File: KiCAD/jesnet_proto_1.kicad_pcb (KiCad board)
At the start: 2 copper layers, 119.5 x 60.6 mm, 163 parts, among them J1 Conn_01x06_Female, J14 Conn_01x06, J15 Conn_01x06, J3 Conn_01x02, J4 Conn_01x01, J5 Rumble, J8 USB_B_Micro, Q1 Q_NMOS_GSD, Q2 Q_PMOS_GDS, Q3 Q_NMOS_GSD, SW1 A, SW10 Dup, SW11 Dright, SW12 Ddown, SW2 B, SW2 L, SW2 R, SW2 Z, SW3 X, SW4 Y, SW5 Start, SW6 L, SW7 R, SW9 Dleft, U1 MCP3202, U10 DRV5055A3xDBZxQ1, U11 DRV5055A3xDBZxQ1, U12 USBLC6-2P6, U13 USBLC6-2P6, U2 Stickbox_Assembly_Main, U3 MCP3202, U4 DRV5055A3xDBZxQ1, U5 Stickbox_Assembly_CStick, U6 AMS1117-3.3, U7 W25Q128JVS, U8 RP2040, U9 DRV5055A3xDBZxQ1, Y1 Crystal_GND24

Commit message: added 3d models to footprints, reversed polarity on trigger sliders
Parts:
- moved C7 2.01 mm to (123.3, 53.8), turned to 180 degrees
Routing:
- net /Lanalog: track 57.9 -> 70.8 mm
- net /Ranalog: track 30.9 -> 33.5 mm
- net GND: track 258.2 -> 256.9 mm

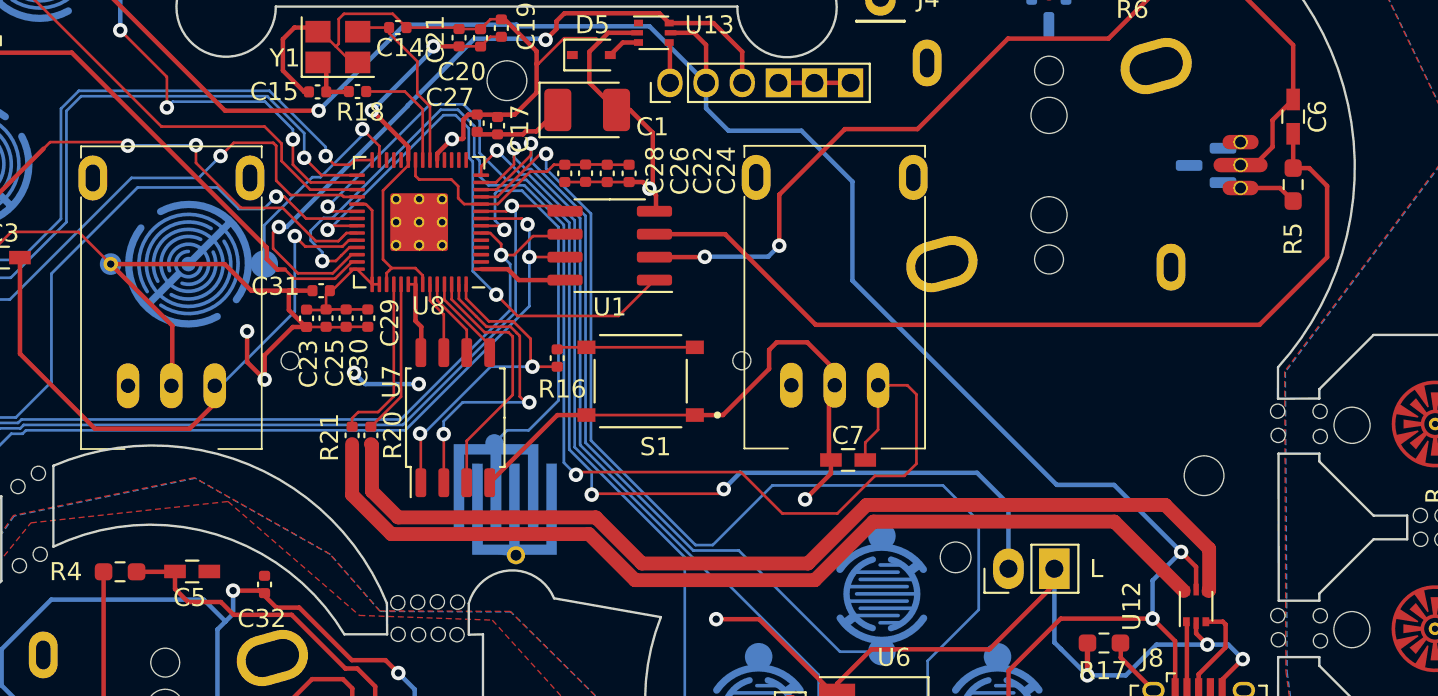
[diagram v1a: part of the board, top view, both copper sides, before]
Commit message: rerouted some traces, fixed 3d model of c0603
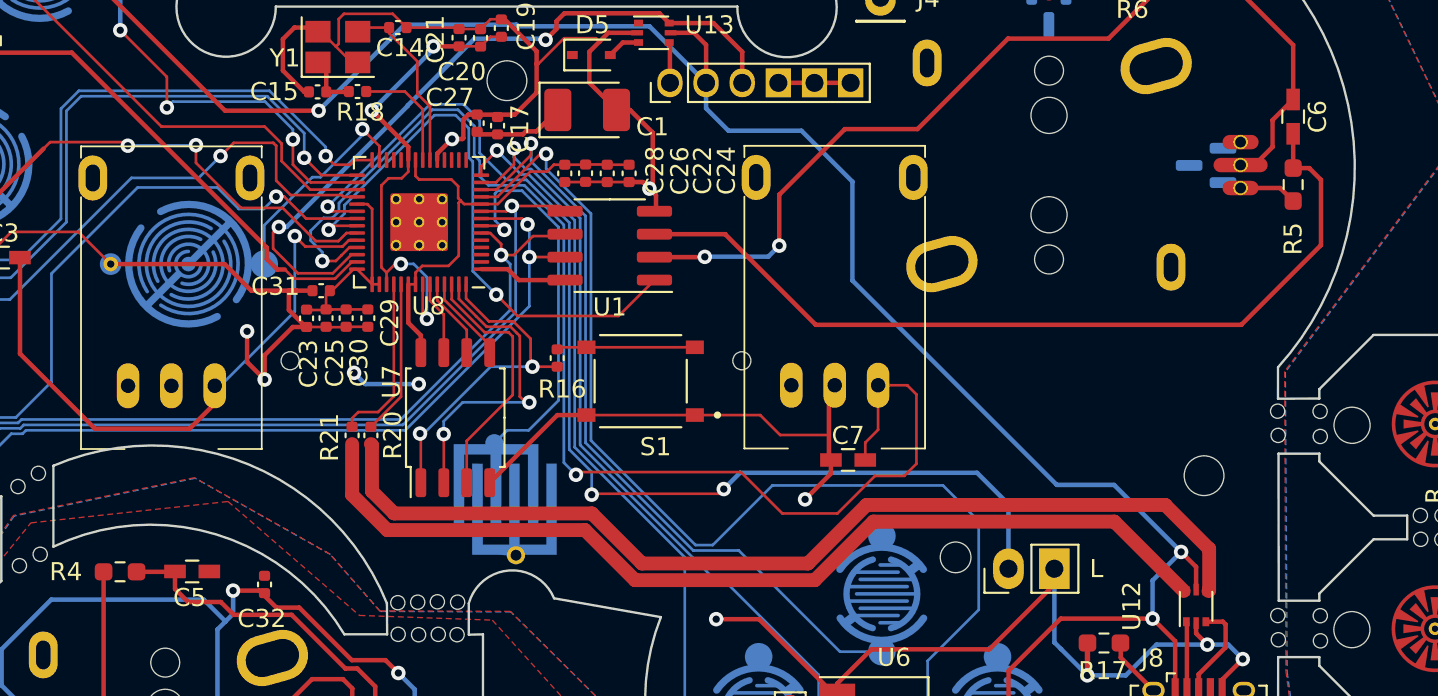
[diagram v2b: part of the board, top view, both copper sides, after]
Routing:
- net GND: track 256.9 -> 245.2 mm
- net +3V3: track 46.3 -> 53.0 mm
- net +1V1: track 22.7 -> 27.6 mm, vias 2 -> 4
- net /Stick_y_filt: track 49.0 -> 48.1 mm

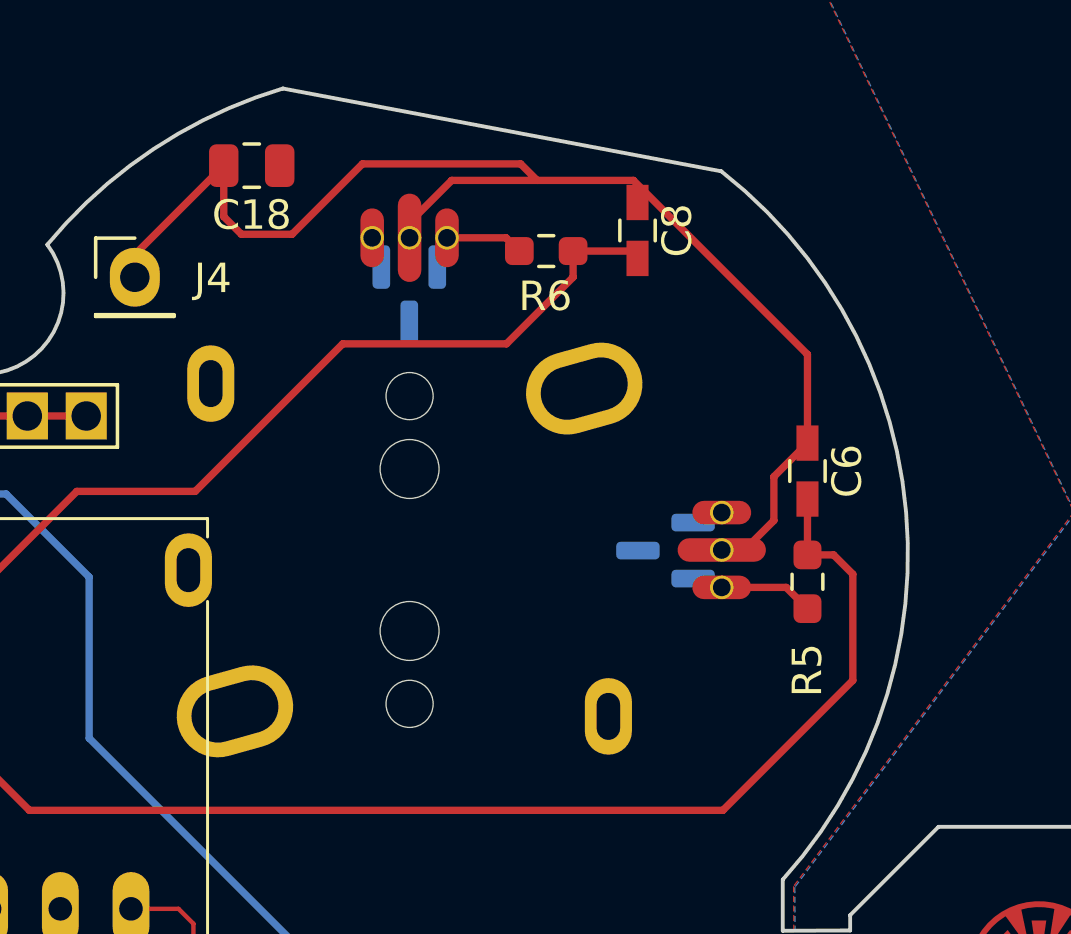
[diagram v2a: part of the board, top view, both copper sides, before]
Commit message: added 3d models, adjusted stickbox positioning
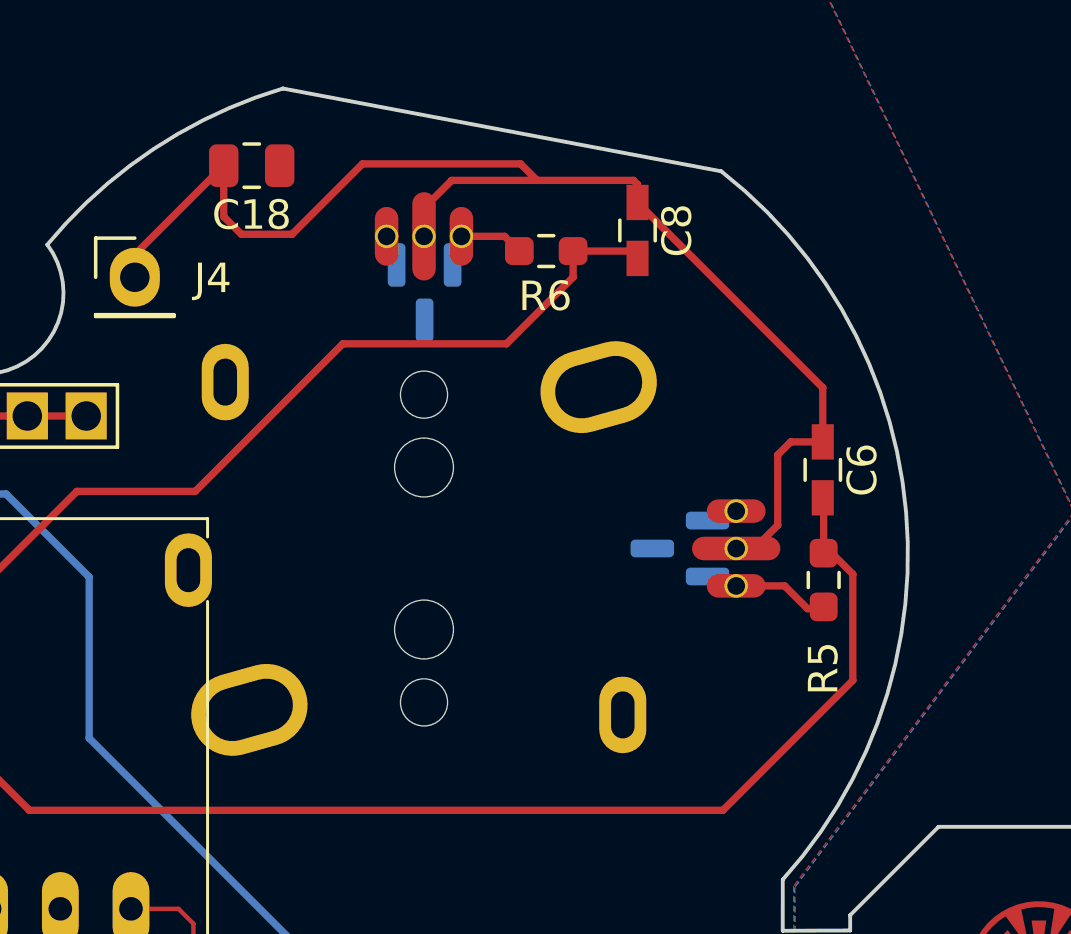
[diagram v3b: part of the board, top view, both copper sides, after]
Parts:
- moved R5 0.55 mm to (148.5, 38.5)
- moved U10 0.52 mm to (134.9, 28.7)
- moved C6 0.52 mm to (148.4, 34.7)
- moved U11 0.49 mm to (143.6, 37.4)
- moved U2 0.49 mm to (134.9, 37.4)
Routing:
- net /Stick_y_filt: track 48.1 -> 47.2 mm

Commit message: final stickbox adjustments
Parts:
- removed the ? at (92.4, 48.3)
- removed H1: 5.2mm, PhobGCC_2_0_0_footprints:MountingHole_5.2mm
- removed H11: MountingHole, PhobGCC_2_0_0_footprints:MountingHole_5.2mm
- removed H12, H13: MountingHole, PhobGCC_2_0_0_footprints:MountingHole_2.0mm
- removed H15: MouseBite, PhobGCC_2_0_0_footprints:breakaway-mousebites-double-v2-large
- removed H2: Slot, PhobGCC_2_0_0_footprints:Slot
- removed H3, H4: 2mm, PhobGCC_2_0_0_footprints:MountingHole_2.0mm
- removed H6: 1.8mm, PhobGCC_2_0_0_footprints:MountingHole_1.8mm
- removed H7: 2.4mm, PhobGCC_2_0_0_footprints:MountingHole_2.4mm
- removed H8: 2.2mm, PhobGCC_2_0_0_footprints:MountingHole_2.2mm
- moved C19 4.19 mm to (100.7, 32.3), turned to 180 degrees
- moved C20 1.68 mm to (101.3, 30.4)
- moved C21 1.58 mm to (100.2, 30.4)
- moved U10 0.56 mm to (134.5, 28.3)
- moved U2 0.55 mm to (134.5, 37.0)
- moved U11 0.52 mm to (143.2, 37.0)
- moved H9 0.30 mm to (142.7, 54.6)
- moved RV2 0.29 mm to (86.1, 49.7)
- moved RV1 0.22 mm to (122.3, 49.6)
- moved SW5 0.19 mm to (104.3, 56.1)
- moved C27 0.14 mm to (102.7, 35.3)
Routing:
- net /Ranalog: track 33.5 -> 27.9 mm
- net +5V: track 175.5 -> 176.6 mm
- net /R: track 31.5 -> 30.5 mm
- net /GCC_DATA: track 40.4 -> 39.5 mm
- net +1V1: track 27.6 -> 26.8 mm
- net /H1YS: track 3.31 -> 4.03 mm
- net /H1XS: track 2.17 -> 2.89 mm
- net +3V3: track 53.0 -> 52.4 mm
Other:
- outline, holes or cut-outs redrawn
